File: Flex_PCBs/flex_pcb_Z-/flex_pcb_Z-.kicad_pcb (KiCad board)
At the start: 2 copper layers, 4.5 x 113.6 mm, 2 parts, among them J1 Conn_01x08_Male, J2 Conn_01x08_Male

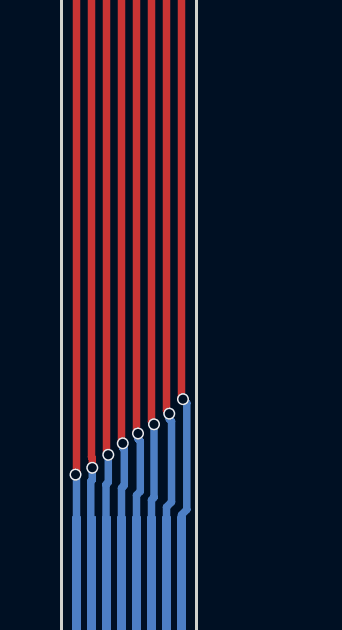
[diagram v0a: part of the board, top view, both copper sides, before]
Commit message: Added small modifications to the existing flex PCBs plus the new ones: Y- and X-.
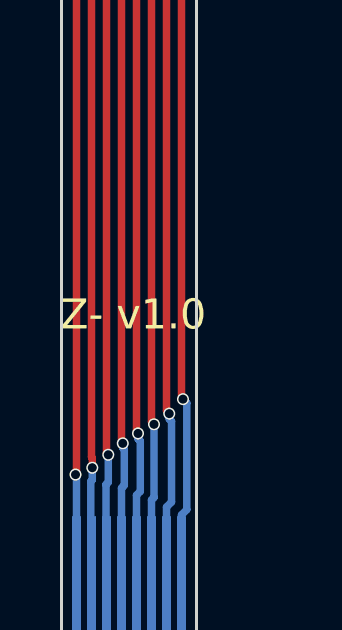
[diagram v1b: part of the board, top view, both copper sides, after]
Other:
- board text added: "Z- v1.0"
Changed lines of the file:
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@@
-(kicad_pcb (version 20211014) (generator pcbnew)
+(kicad_pcb (version 20221018) (generator pcbnew)
   (general
     (thickness 1.6)
@@
     (pcbplotparams
       (layerselection 0x00410fc_ffffffff)
+      (plot_on_all_layers_selection 0x0000000_00000000)
       (disableapertmacros false)
       (usegerberextensions true)
@@
       (usegerberadvancedattributes false)
       (creategerberjobfile false)
-      (svguseinch false)
+      (dashed_line_dash_ratio 12.000000)
+      (dashed_line_gap_ratio 3.000000)
       (svgprecision 6)
-      (excludeedgelayer true)
       (plotframeref false)
       (viasonmask false)
@@
       (drillshape 0)
       (scaleselection 1)
-      (outputdirectory "gerber_Z-/")
+      (outputdirectory "/home/stefan/DEV/spaceteam/gerber/Z-/")
     )
   )
@@
     (attr smd)
     (fp_text reference "J1" (at -16.51 -3.81 unlocked) (layer "F.SilkS") hide
-      (effects (font (size 1 1) (thickness 0.15)))
+        (effects (font (size 1 1) (thickness 0.15)))
     )
     (fp_text value "Conn_01x08_Male" (at -16.51 -2.31 unlocked) (layer "F.Fab")
-      (effects (font (size 1 1) (thickness 0.15)))
+        (effects (font (size 1 1) (thickness 0.15)))
     )
     (fp_text user "${REFERENCE}" (at -16.51 -0.81 unlocked) (layer "F.Fab")
-      (effects (font (size 1 1) (thickness 0.15)))
+        (effects (font (size 1 1) (thickness 0.15)))
     )
     (pad "1" smd rect (at 0.5 -2) (size 0.3 4) (layers "F.Cu" "F.Paste" "F.Mask")
@@
     (attr smd)
     (fp_text reference "J2" (at -16.51 3.81 unlocked) (layer "B.SilkS") hide
-      (effects (font (size 1 1) (thickness 0.15)) (justify mirror))
+        (effects (font (size 1 1) (thickness 0.15)) (justify mirror))
     )
     (fp_text value "Conn_01x08_Male" (at -16.51 2.31 unlocked) (layer "B.Fab")
-      (effects (font (size 1 1) (thickness 0.15)) (justify mirror))
+        (effects (font (size 1 1) (thickness 0.15)) (justify mirror))
     )
     (fp_text user "${REFERENCE}" (at -16.51 0.81 unlocked) (layer "B.Fab")
-      (effects (font (size 1 1) (thickness 0.15)) (justify mirror))
+        (effects (font (size 1 1) (thickness 0.15)) (justify mirror))
     )
     (pad "1" smd rect (at 0.5 2 180) (size 0.3 4) (layers "B.Cu" "B.Paste" "B.Mask")
@@
       (net 1 "8") (pinfunction "Pin_8") (pintype "passive"))
   )
-  (gr_line (start 107 50) (end 111.5 50) (layer "Edge.Cuts") (width 0.1))
-  (gr_line (start 107 50) (end 107 163.6) (layer "Edge.Cuts") (width 0.1))
-  (gr_line (start 111.5 50) (end 111.5 163.6) (layer "Edge.Cuts") (width 0.1))
-  (gr_line (start 107 163.6) (end 111.5 163.6) (layer "Edge.Cuts") (width 0.1))
-  (gr_rect (start 107 59.26) (end 111.5 50) (layer "User.1") (width 0.15) (fill none))
-  (gr_rect (start 107 163.6) (end 111.5 154.34) (layer "User.1") (width 0.15) (fill none))
+  (gr_line (start 107 50) (end 111.5 50)
+    (stroke (width 0.1) (type solid)) (layer "Edge.Cuts"))
+  (gr_line (start 107 50) (end 107 163.6)
+    (stroke (width 0.1) (type solid)) (layer "Edge.Cuts"))
+  (gr_line (start 111.5 50) (end 111.5 163.6)
+    (stroke (width 0.1) (type solid)) (layer "Edge.Cuts"))
+  (gr_line (start 107 163.6) (end 111.5 163.6)
+    (stroke (width 0.1) (type solid)) (layer "Edge.Cuts"))
+  (gr_rect (start 107 50) (end 111.5 59.26)
+    (stroke (width 0.15) (type solid)) (fill none) (layer "User.1"))
+  (gr_rect (start 107 154.34) (end 111.5 163.6)
+    (stroke (width 0.15) (type solid)) (fill none) (layer "User.1"))
+  (gr_text "Z- v1.0" (at 106.9594 153.3652) (layer "F.SilkS")
+    (effects (font (size 1 1) (thickness 0.15)) (justify left bottom))
+  )
   (gr_text "The PCB should have \na thickness of 0.12 mm (two Layer).\nOn the marked areas in User.1 layer a 0.225 mm polyimide stiffener\nshould be glued.\nThe resulting gold fingers should have 0.3 mm in thickness.\n\n\n" (at 92.1258 169.2402) (layer "User.1")
     (effects (font (size 1 1) (thickness 0.15)))
